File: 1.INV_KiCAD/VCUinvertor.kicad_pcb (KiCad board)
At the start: 2 copper layers, 100.7 x 117.9 mm, 118 parts, among them J7 PowerSupply, J9 BRAKE LIGHT, Q1 2N7002, Q10 2N7002, Q11 BC848C, Q12 BCP51, Q2 2N7002, Q3 2N7002, Q4 2N7002, Q5 2N7002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

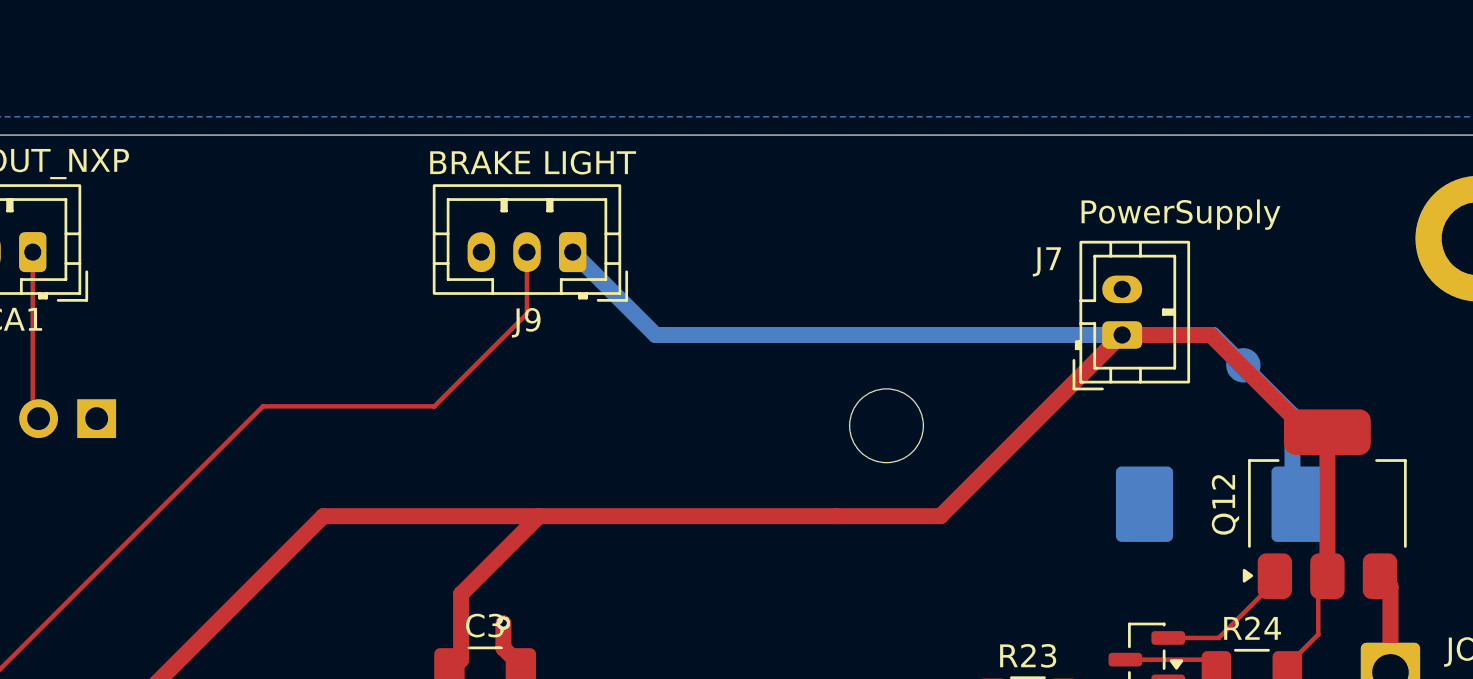
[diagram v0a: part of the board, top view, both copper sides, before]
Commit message: Redid reverse polarity protection
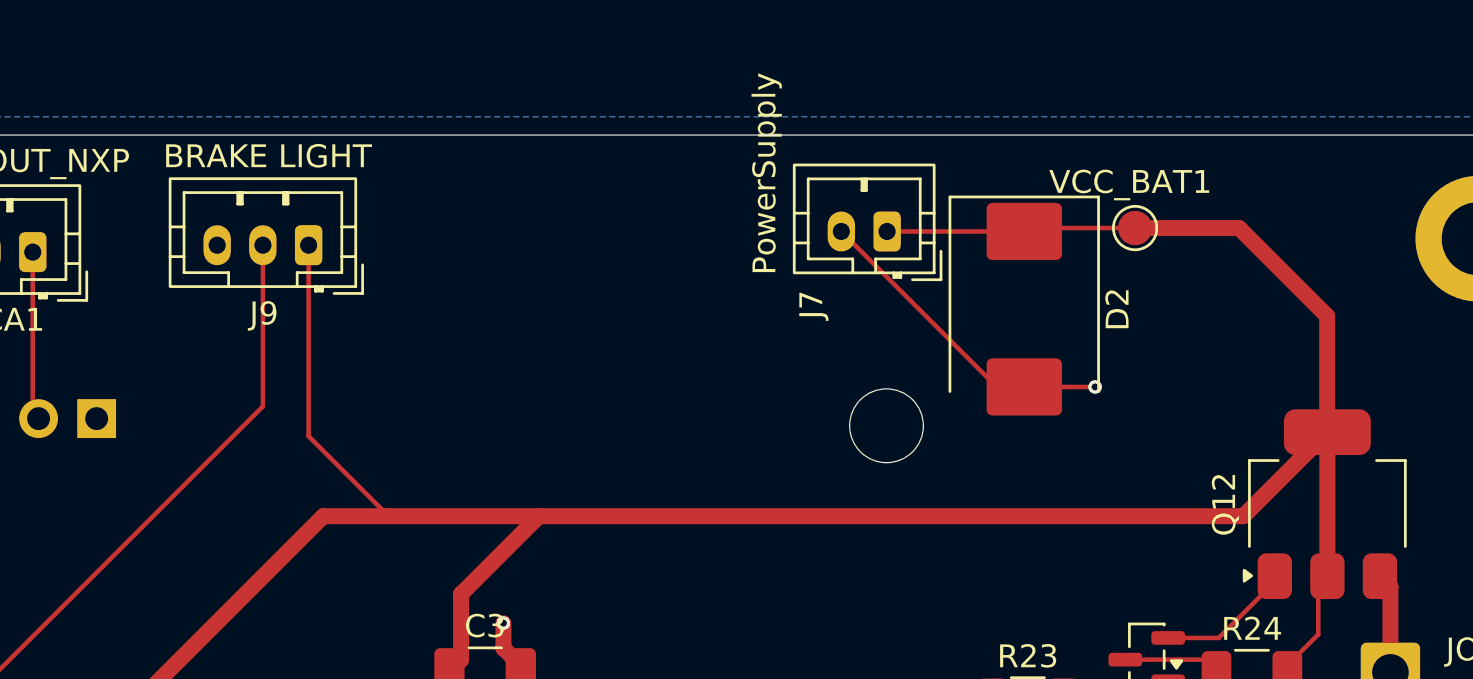
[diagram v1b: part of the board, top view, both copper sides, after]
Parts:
- D2, VCC_BAT1: moved to F.Cu
- moved D2 12.2 mm to (125.0, 56.6), turned to -90 degrees
- moved J9 11.6 mm to (93.7, 53.8)
- moved J7 11.2 mm to (119.0, 53.2), turned to 180 degrees
- moved VCC_BAT1 7.64 mm to (129.9, 53.1), turned to 0 degrees
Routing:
- net GND: track 64.6 -> 78.5 mm, vias 26 -> 27
- net BRAKELIGHT: track 56.3 -> 47.4 mm
- net BAT+: track 151.0 -> 149.7 mm

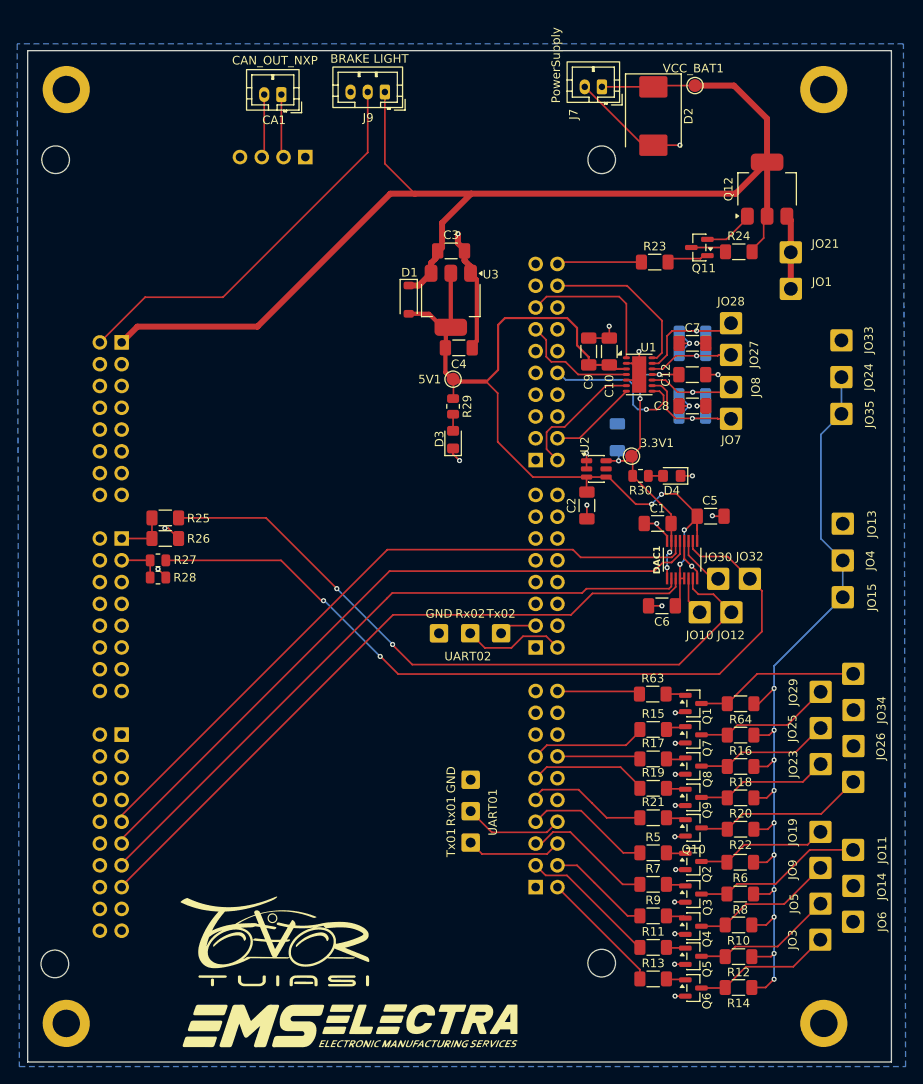
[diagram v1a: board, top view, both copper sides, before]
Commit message: Supply GND small correction
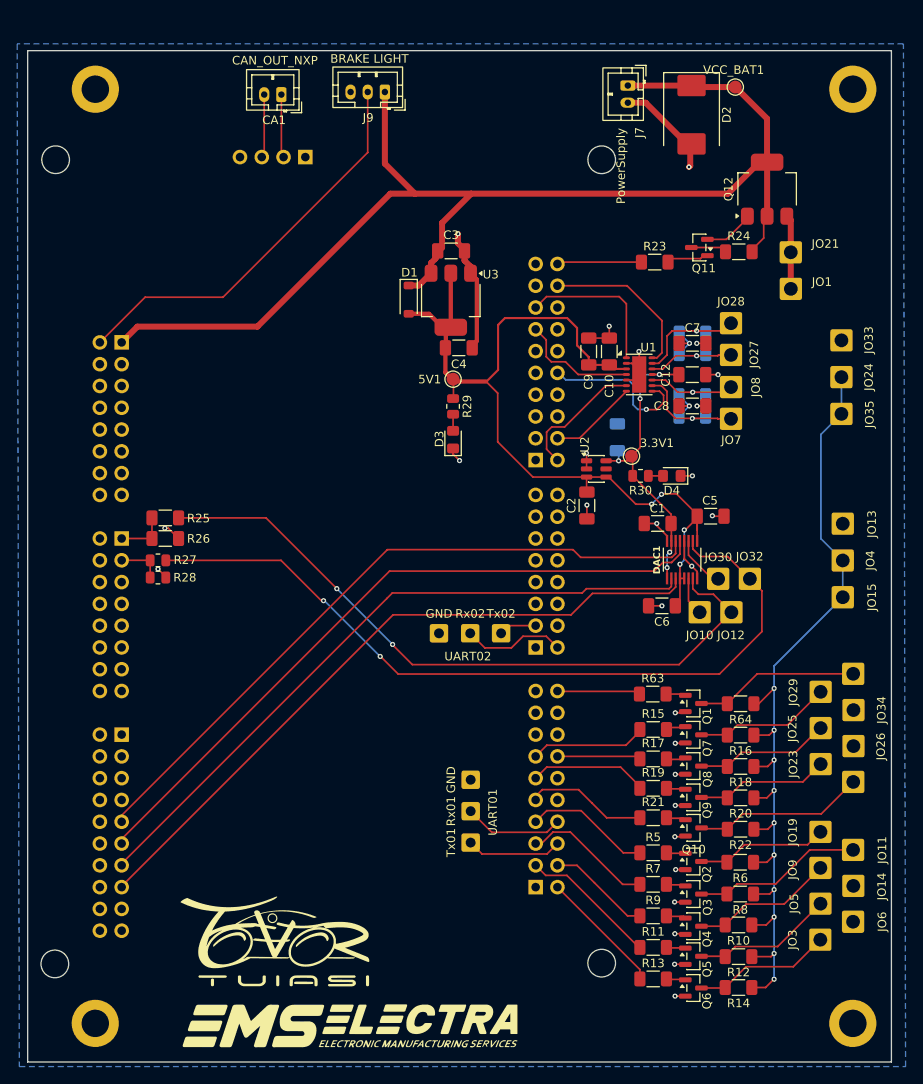
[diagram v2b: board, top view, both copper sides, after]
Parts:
- moved VCC_BAT1 4.70 mm to (134.6, 53.3)
- moved D2 4.45 mm to (129.5, 56.5)
- moved H1 3.39 mm to (148.3, 53.5)
- moved H2 3.39 mm to (60.0, 53.5)
- moved H3 3.38 mm to (59.9, 162.4)
- moved H4 3.38 mm to (148.3, 162.4)
- moved J7 3.03 mm to (122.0, 53.1), turned to -90 degrees
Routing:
- net BAT+: track 149.7 -> 146.9 mm
- net GND: track 78.5 -> 76.8 mm

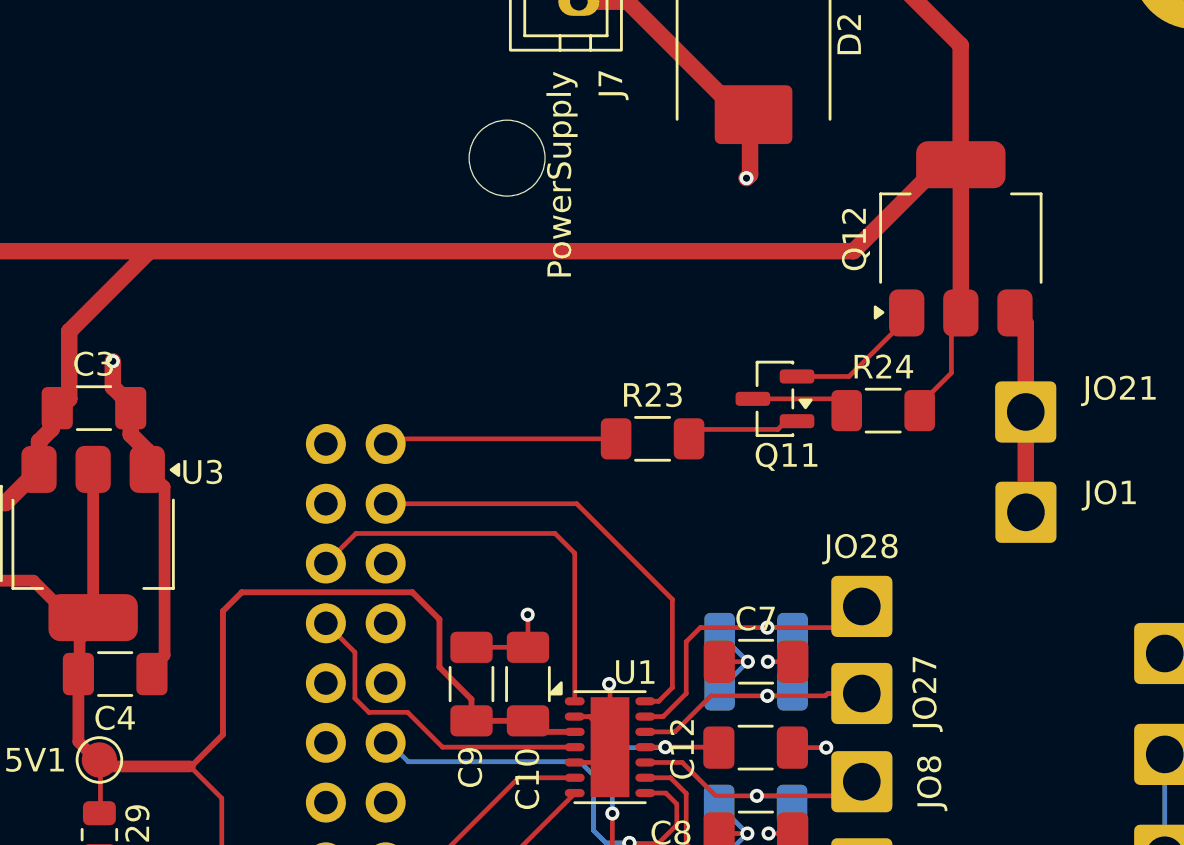
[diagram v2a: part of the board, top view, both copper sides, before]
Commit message: Dorlington -> Relay for INV_OFF
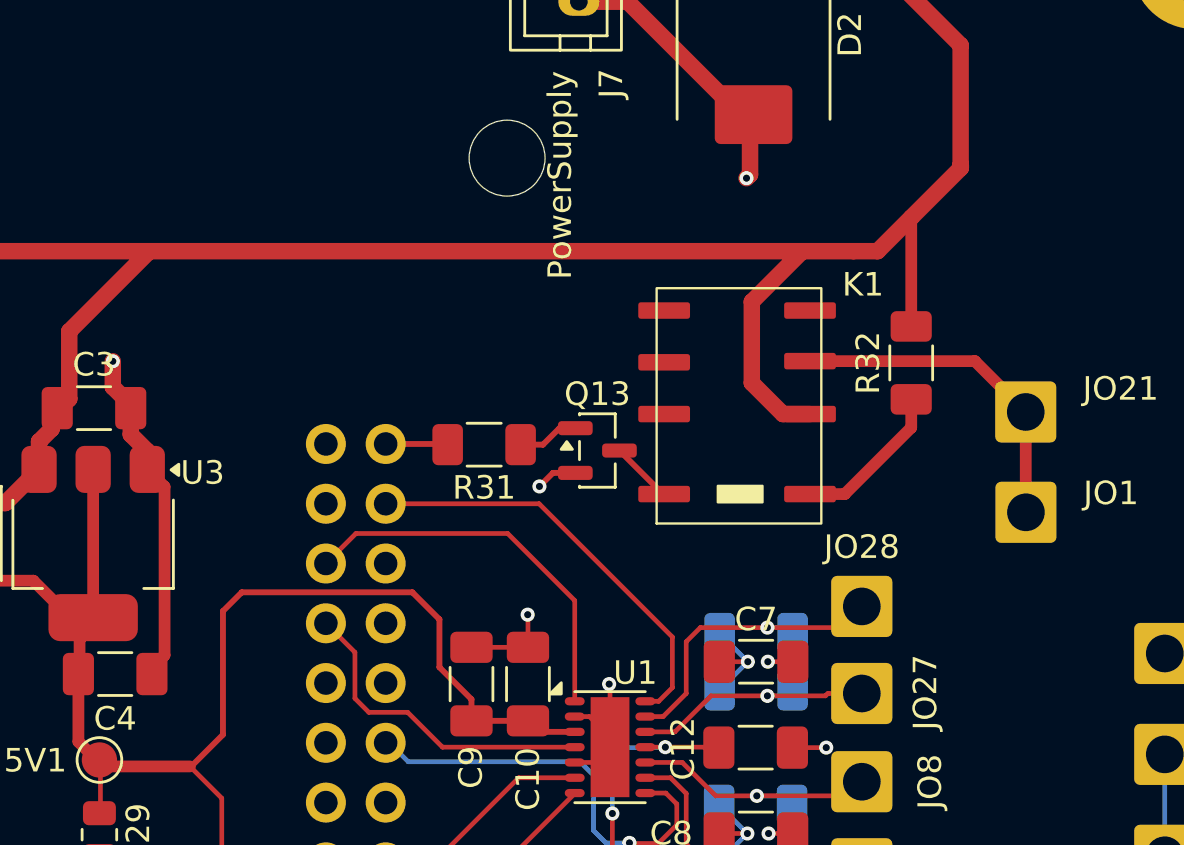
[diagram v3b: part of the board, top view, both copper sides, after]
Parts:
- removed Q11: BC848C, Package_TO_SOT_SMD:SOT-23
- removed Q12: BCP51, Package_TO_SOT_SMD:SOT-223-3_TabPin2
- removed R23: 1.7k, Resistor_SMD:R_1206_3216Metric_Pad1.30x1.75mm_HandSolder
- removed R24: 360R, Resistor_SMD:R_1206_3216Metric_Pad1.30x1.75mm_HandSolder
- added K1: IM06, Library_GHST:Relay_IM06DGR, F.Cu at (126.7, 71.9)
- added Q13: BC848C, Package_TO_SOT_SMD:SOT-23, F.Cu at (122.8, 74.2)
- added R31: 1k, Resistor_SMD:R_1206_3216Metric_Pad1.30x1.75mm_HandSolder, F.Cu at (118.0, 73.9)
- added R32: 360R, Resistor_SMD:R_1206_3216Metric_Pad1.30x1.75mm_HandSolder, F.Cu at (136.2, 70.4)
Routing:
- net INV_OFF: track 9.88 -> 2.65 mm
- net Net-(K1-Pad1): track 0.00 -> 6.67 mm
- net Net-(Q11-E): track 5.93 -> 0.00 mm
- net /INV_Supply: track 8.67 -> 14.3 mm
- net Net-(Q11-B): track 4.90 -> 0.00 mm
- net Net-(Q11-C): track 4.19 -> 0.00 mm
- net Net-(Q13-C): track 0.00 -> 2.67 mm
- net Net-(Q13-B): track 0.00 -> 2.61 mm
- net BAT+: track 146.9 -> 149.1 mm
- net GND: track 76.8 -> 78.6 mm, vias 27 -> 28
- net /TX1: track 17.7 -> 16.6 mm
- net /Pyy: track 19.0 -> 18.1 mm

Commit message: Block diagram cleanUp
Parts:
- moved JO1 5.68 mm to (146.7, 76.8)
- moved JO21 5.68 mm to (146.7, 72.5)
- moved R32 5.43 mm to (141.6, 70.5)
- moved K1 4.70 mm to (131.4, 71.8)
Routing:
- net BAT+: track 149.1 -> 158.1 mm
- net Net-(Q13-C): track 2.67 -> 7.36 mm
- net /INV_Supply: track 14.3 -> 15.3 mm
- net +5V: track 105.8 -> 105.1 mm

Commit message: Simulations_continued
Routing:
- net Net-(CA0-Pin_3): track 7.40 -> 8.09 mm
- net Net-(CA0-Pin_2): track 7.39 -> 8.04 mm
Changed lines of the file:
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@@
 		(tags "capacitor handsolder")
 		(property "Reference" "C8"
-			(at 3.6 0 0)
+			(at -0.06 -2 0)
 			(layer "F.SilkS")
 			(effects
@@
 		(at 131.35051 71.84274 90)
 		(property "Reference" "K1"
-			(at 4.75 7.45 0)
+			(at 5.5 2.725 0)
 			(unlocked yes)
 			(layer "F.SilkS")
@@
 		(tags "test point SMD pad")
 		(property "Reference" "VCC_BAT1"
-			(at -0.2 -2 0)
+			(at 2.81 -2.015 0)
 			(layer "F.SilkS")
 			(effects
@@
 		)
 		(fp_text user "${REFERENCE}"
-			(at -0.325 -2.05 0)
+			(at 0.08 -2.885 0)
 			(layer "F.Fab")
 			(effects
@@
 		)
 		(fill hatch)
+		(locked yes)
 		(layer "B.Paste")
 	)
@@
 		)
 		(fill no)
+		(locked yes)
 		(layer "B.Paste")
 	)
@@
 	)
 	(gr_text "Brk_AN (Brown)"
+		(locked yes)
 		(at 124.435099 111.617401 90)
 		(layer "B.Paste")
@@
 	)
 	(gr_text "TPS (Green)"
+		(locked yes)
 		(at 126.035995 110.307877 90)
 		(layer "B.Paste")
@@
 	)
 	(segment
-		(start 81.88879 61.427751)
-		(end 81.6343 61.173261)
+		(start 81.6343 54.35895)
+		(end 80.85051 55.14274)
+		(width 0.2)
+		(layer "F.Cu")
+		(net "Net-(CA0-Pin_2)")
+	)
+	(segment
+		(start 81.88879 61.38102)
+		(end 81.88879 61.427751)
+		(width 0.2)
+		(layer "F.Cu")
+		(net "Net-(CA0-Pin_2)")
+	)
+	(segment
+		(start 80.85051 55.14274)
+		(end 80.85051 60.34274)
+		(width 0.2)
+		(layer "F.Cu")
+		(net "Net-(CA0-Pin_2)")
+	)
+	(segment
+		(start 80.85051 60.34274)
+		(end 81.88879 61.38102)
 		(width 0.2)
 		(layer "F.Cu")
@@
 	)
 	(segment
-		(start 81.6343 61.173261)
-		(end 81.6343 54.145491)
+		(start 81.6343 54.145491)
+		(end 81.6343 54.35895)
 		(width 0.2)
 		(layer "F.Cu")
@@
 	)
 	(segment
-		(start 79.634299 61.142242)
-		(end 79.634299 54.145491)
+		(start 79.65051 54.161702)
+		(end 79.65051 54.34274)
+		(width 0.2)
+		(layer "F.Cu")
+		(net "Net-(CA0-Pin_3)")
+	)
+	(segment
+		(start 80.45051 60.34274)
+		(end 79.365499 61.427751)
+		(width 0.2)
+		(layer "F.Cu")
+		(net "Net-(CA0-Pin_3)")
+	)
+	(segment
+		(start 79.365499 61.427751)
+		(end 79.34879 61.427751)
+		(width 0.2)
+		(layer "F.Cu")
+		(net "Net-(CA0-Pin_3)")
+	)
+	(segment
+		(start 80.45051 55.14274)
+		(end 80.45051 60.34274)
 		(width 0.2)
 		(layer "F.Cu")
@@
 	)
 	(segment
-		(start 79.34879 61.427751)
-		(end 79.634299 61.142242)
+		(start 79.65051 54.34274)
+		(end 80.45051 55.14274)
+		(width 0.2)
+		(layer "F.Cu")
+		(net "Net-(CA0-Pin_3)")
+	)
+	(segment
+		(start 79.634299 54.145491)
+		(end 79.65051 54.161702)
 		(width 0.2)
 		(layer "F.Cu")
@@
 		(net "GND")
 		(layer "B.Cu")
+		(name "AGND")
+		(hatch edge 0.5)
+		(priority 1)
+		(connect_pads
+			(clearance 0)
+		)
+		(min_thickness 0.25)
+		(fill yes
+			(thermal_gap 0.5)
+			(thermal_bridge_width 0.5)
+			(island_removal_mode 1)
+		)
+		(polygon
+			(pts
+				(xy 138.07051 101.48274) (xy 139.321817 104.014111) (xy 139.319204 116.363983) (xy 135.07051 121.25274)
+				(xy 132.12051 122.32274) (xy 118.306142 122.421676) (xy 118.28051 118.84274) (xy 128.20051 118.42274)
+				(xy 128.56051 109.551063) (xy 128.515526 104.063958) (xy 128.59051 102.37274) (xy 130.89051 101.44274)
+				(xy 135.08051 101.39274)
+			)
+		)
+	)
+	(zone
+		(net "GND")
+		(layer "B.Cu")
 		(hatch edge 0.5)
 		(connect_pads
@@
 		(polygon
 			(pts
-				(xy 50.83379 48.227751) (xy 51.08379 167.452751) (xy 154.400505 167.452751) (xy 154.150505 48.227751)
+				(xy 154.400505 167.452751) (xy 51.08379 167.452751) (xy 50.83379 48.227751) (xy 154.150505 48.227751)
+			)
+		)
+		(polygon
+			(pts
+				(xy 127.952178 102.080864) (xy 127.63051 117.90274) (xy 118.00051 118.58274) (xy 117.85051 122.84274)
+				(xy 132.65051 122.84274) (xy 135.65051 121.44274) (xy 139.75051 117.74274) (xy 139.92051 115.51274)
+				(xy 139.965018 115.260003) (xy 140.04051 114.73274) (xy 140.036278 113.517532) (xy 140.09051 112.37274)
+				(xy 140.05051 111.49274) (xy 139.93051 102.79274) (xy 138.19051 101.00274) (xy 130.26938 100.864333)
 			)
 		)
